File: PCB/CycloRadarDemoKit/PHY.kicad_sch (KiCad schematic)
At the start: 34 parts, among them J201 ARJM11B1-009-AB-EW2, U201 IP101GRI, Y201 25MHz

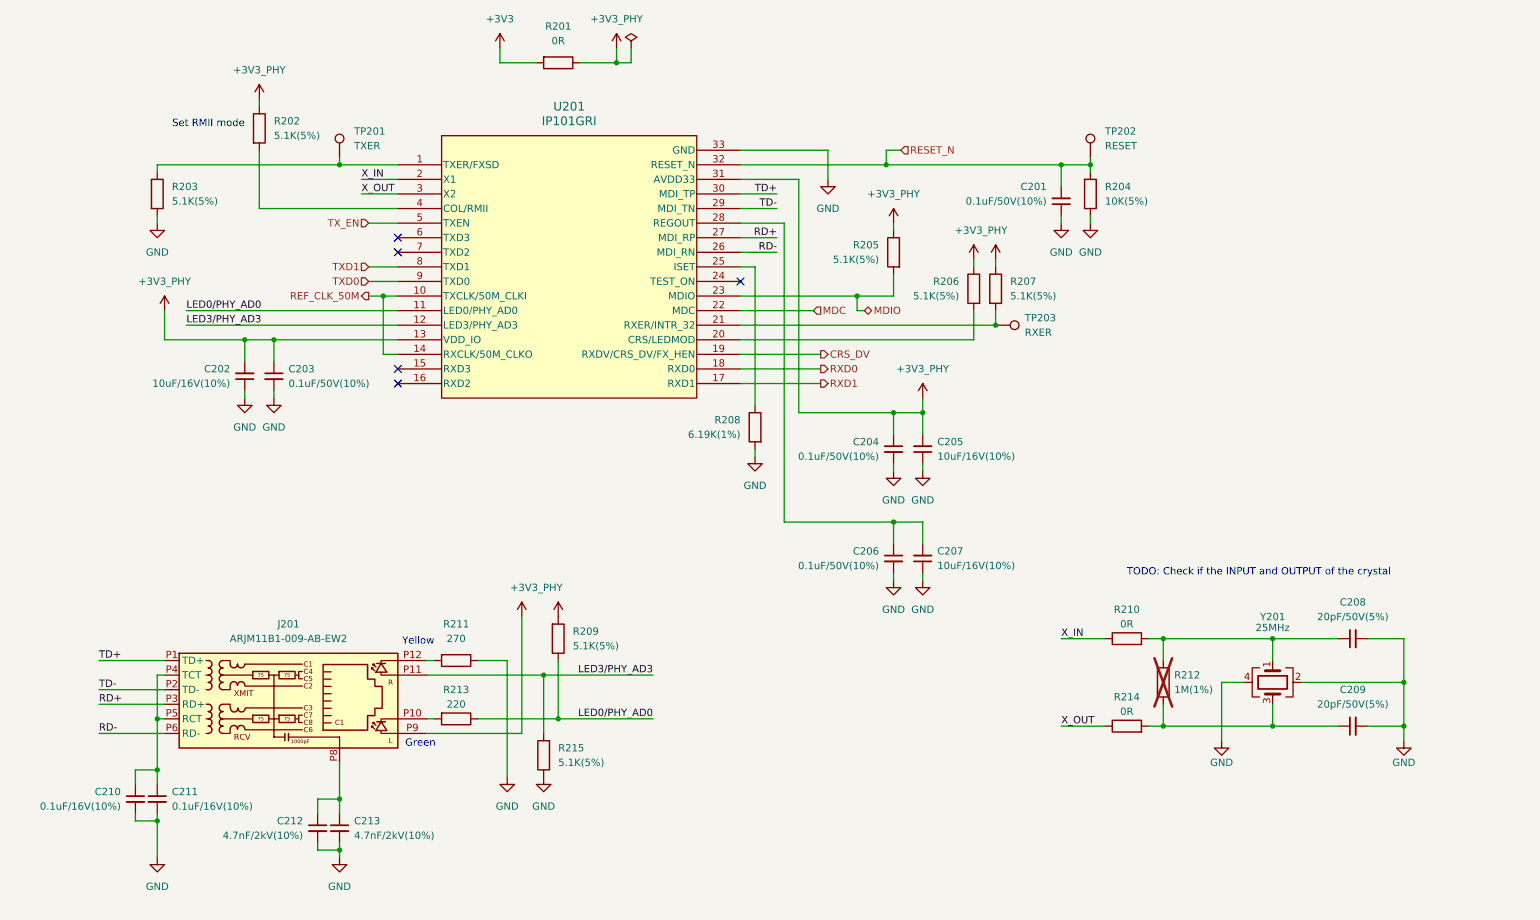
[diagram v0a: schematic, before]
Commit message: added buzzer and pins for Radar
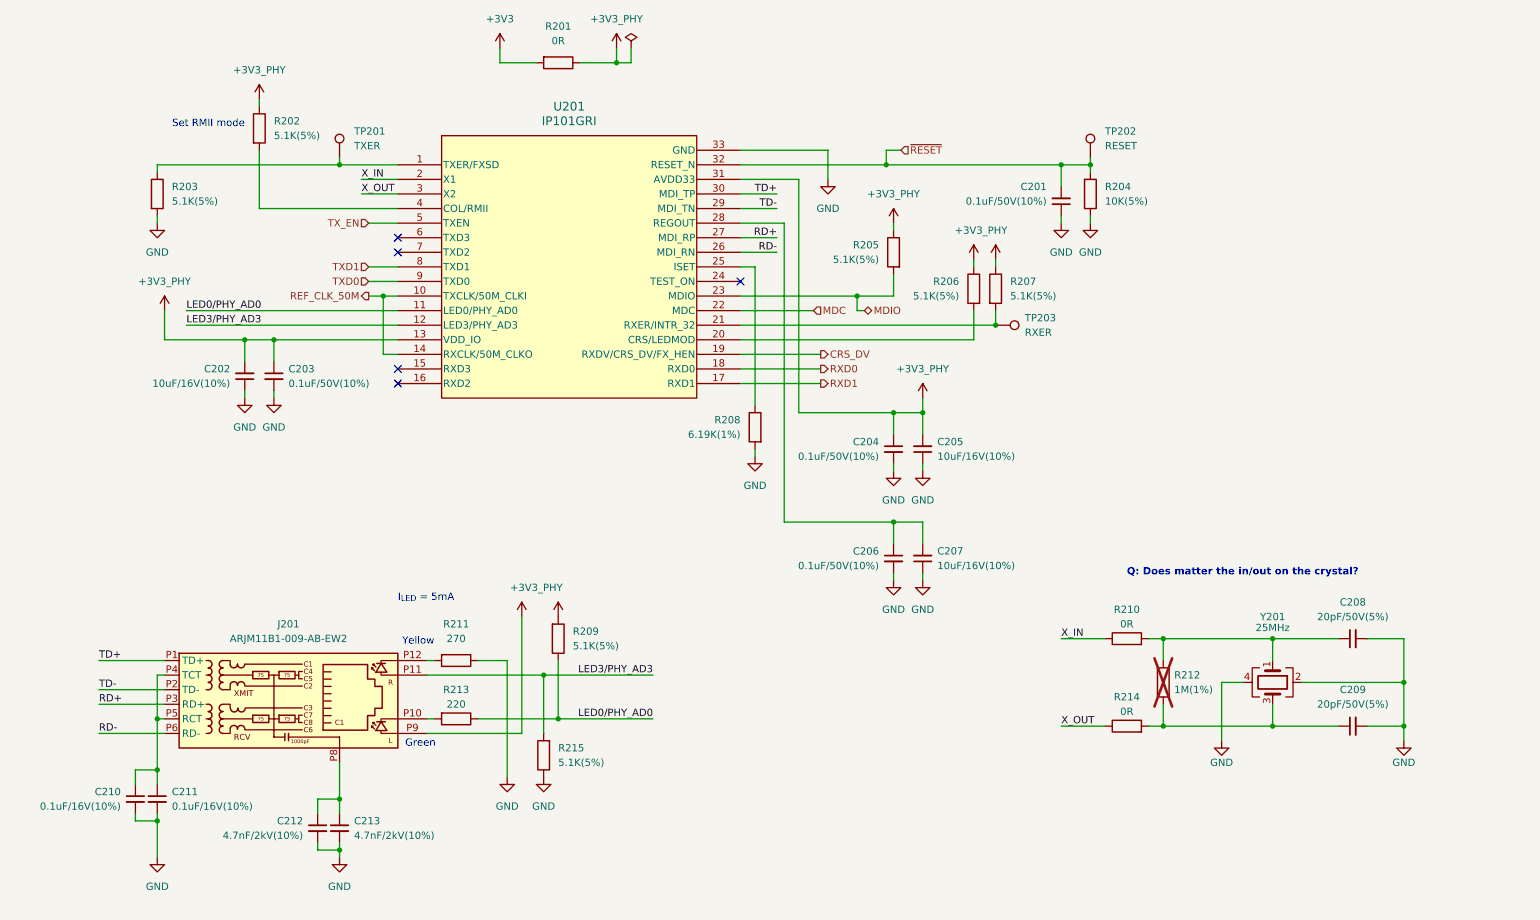
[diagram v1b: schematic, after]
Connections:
- net RESET_N renamed ~{RESET}
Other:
- note added: "I_{LED} = 5mA"
- note added: "Q: Does matter the in/out on the crystal?"
- note removed: "TODO: Check if the INPUT and OUTPUT of the crystal"
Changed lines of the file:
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@@
+    (effects (font (size 1.27 1.27)) (justify left bottom))
+  )
+  (text "I_{LED} = 5mA" (at 91.44 125.73 0)
     (effects (font (size 1.27 1.27)) (justify left bottom))
   )
@@
     (effects (font (size 1.27 1.27)) (justify right bottom))
   )
-  (text "TODO: Check if the INPUT and OUTPUT of the crystal"
-    (at 218.44 121.285 0)
-    (effects (font (size 1.27 1.27)) (justify left bottom))
+  (text "Q: Does matter the in/out on the crystal?" (at 218.44 121.285 0)
+    (effects (font (size 1.27 1.27) (thickness 0.254) bold) (justify left bottom))
   )
   (label "X_IN" (at 85.09 52.07 0) (fields_autoplaced)
@@
     (effects (font (size 1.27 1.27)) (justify right))
   )
-  (hierarchical_label "RESET_N" (shape input) (at 179.07 46.99 0) (fields_autoplaced)
+  (hierarchical_label "~{RESET}" (shape input) (at 179.07 46.99 0) (fields_autoplaced)
     (effects (font (size 1.27 1.27)) (justify left))
   )

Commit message: more components fthprnt added
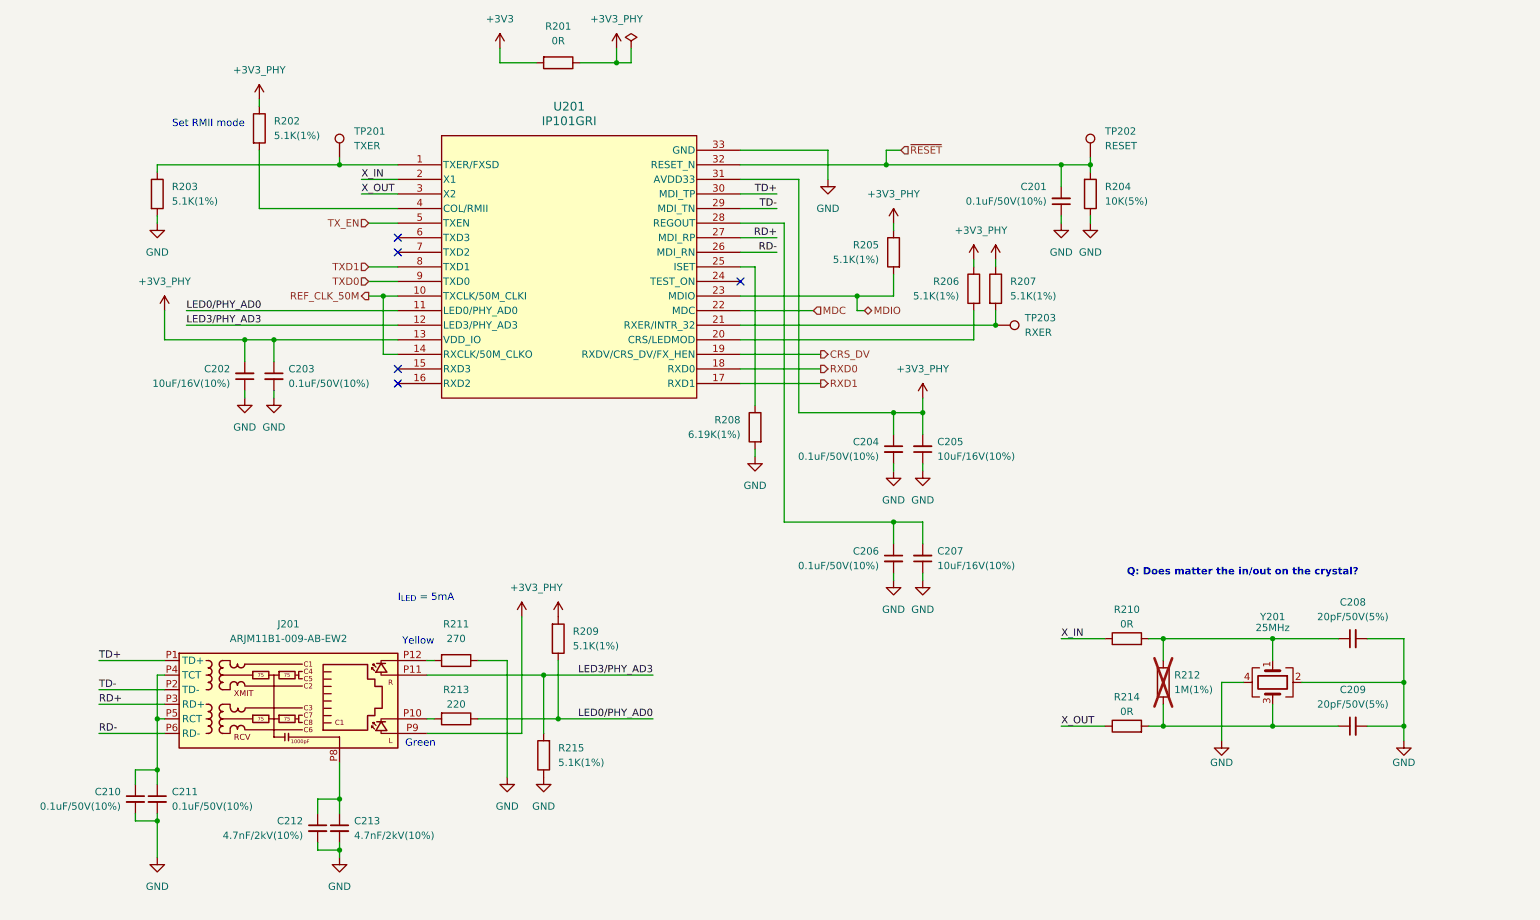
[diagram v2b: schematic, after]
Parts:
- C210, C211: value 0.1uF/16V(10%) -> 0.1uF/50V(10%); footprint (none) -> Capacitor_SMD:C_0603_1608Metric; LCSC (none) -> C14663
- R202, R203, R205, R206, R207, R209, R215: value 5.1K(5%) -> 5.1K(1%); footprint (none) -> Resistor_SMD:R_0603_1608Metric; LCSC (none) -> C23186
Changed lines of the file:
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@@
       (effects (font (size 1.27 1.27)) (justify right))
     )
-    (property "Value" "5.1K(5%)" (at 119.38 153.67 0)
+    (property "Value" "5.1K(1%)" (at 119.38 153.67 0)
       (effects (font (size 1.27 1.27)) (justify right))
     )
-    (property "Footprint" "" (at 118.618 152.4 90)
+    (property "Footprint" "Resistor_SMD:R_0603_1608Metric" (at 118.618 152.4 90)
       (effects (font (size 1.27 1.27)) hide)
     )
@@
       (effects (font (size 1.27 1.27)) hide)
     )
+    (property "LCSC" "C23186" (at 116.84 152.4 0)
+      (effects (font (size 1.27 1.27)) hide)
+    )
     (pin "1")
     (pin "2")
@@
       (effects (font (size 1.27 1.27)) (justify left))
     )
-    (property "Value" "5.1K(5%)" (at 121.92 133.35 0)
-      (effects (font (size 1.27 1.27)) (justify left))
-    )
-    (property "Footprint" "" (at 117.602 132.08 90)
+    (property "Value" "5.1K(1%)" (at 121.92 133.35 0)
+      (effects (font (size 1.27 1.27)) (justify left))
+    )
+    (property "Footprint" "Resistor_SMD:R_0603_1608Metric" (at 117.602 132.08 90)
       (effects (font (size 1.27 1.27)) hide)
     )
     (property "Datasheet" "~" (at 119.38 132.08 0)
+      (effects (font (size 1.27 1.27)) hide)
+    )
+    (property "LCSC" "C23186" (at 119.38 132.08 0)
       (effects (font (size 1.27 1.27)) hide)
     )
@@
       (effects (font (size 1.27 1.27)) (justify left))
     )
-    (property "Value" "5.1K(5%)" (at 175.26 66.04 0)
-      (effects (font (size 1.27 1.27)) (justify left))
-    )
-    (property "Footprint" "" (at 179.578 64.77 90)
+    (property "Value" "5.1K(1%)" (at 175.26 66.04 0)
+      (effects (font (size 1.27 1.27)) (justify left))
+    )
+    (property "Footprint" "Resistor_SMD:R_0603_1608Metric" (at 179.578 64.77 90)
       (effects (font (size 1.27 1.27)) hide)
     )
@@
       (effects (font (size 1.27 1.27)) hide)
     )
+    (property "LCSC" "C23186" (at 177.8 64.77 0)
+      (effects (font (size 1.27 1.27)) hide)
+    )
     (pin "1")
     (pin "2")
@@
       (effects (font (size 1.27 1.27)) (justify left))
     )
-    (property "Value" "5.1K(5%)" (at 52.07 55.88 0)
-      (effects (font (size 1.27 1.27)) (justify left))
-    )
-    (property "Footprint" "" (at 47.752 54.61 90)
+    (property "Value" "5.1K(1%)" (at 52.07 55.88 0)
+      (effects (font (size 1.27 1.27)) (justify left))
+    )
+    (property "Footprint" "Resistor_SMD:R_0603_1608Metric" (at 47.752 54.61 90)
       (effects (font (size 1.27 1.27)) hide)
     )
     (property "Datasheet" "~" (at 49.53 54.61 0)
+      (effects (font (size 1.27 1.27)) hide)
+    )
+    (property "LCSC" "C23186" (at 49.53 54.61 0)
       (effects (font (size 1.27 1.27)) hide)
     )
@@
       (effects (font (size 1.27 1.27)) (justify left))
     )
-    (property "Value" "5.1K(5%)" (at 198.12 72.39 0)
-      (effects (font (size 1.27 1.27)) (justify left))
-    )
-    (property "Footprint" "" (at 193.802 71.12 90)
+    (property "Value" "5.1K(1%)" (at 198.12 72.39 0)
+      (effects (font (size 1.27 1.27)) (justify left))
+    )
+    (property "Footprint" "Resistor_SMD:R_0603_1608Metric" (at 193.802 71.12 90)
       (effects (font (size 1.27 1.27)) hide)
     )
     (property "Datasheet" "~" (at 195.58 71.12 0)
+      (effects (font (size 1.27 1.27)) hide)
+    )
+    (property "LCSC" "C23186" (at 195.58 71.12 0)
       (effects (font (size 1.27 1.27)) hide)
     )
@@
       (effects (font (size 1.27 1.27)) (justify left))
     )
-    (property "Value" "0.1uF/16V(10%)" (at 52.07 161.2963 0)
-      (effects (font (size 1.27 1.27)) (justify left))
-    )
-    (property "Footprint" "" (at 49.53 160.02 0)
+    (property "Value" "0.1uF/50V(10%)" (at 52.07 161.2963 0)
+      (effects (font (size 1.27 1.27)) (justify left))
+    )
+    (property "Footprint" "Capacitor_SMD:C_0603_1608Metric" (at 49.53 160.02 0)
       (effects (font (size 1.27 1.27)) hide)
     )
     (property "Datasheet" "~" (at 49.53 160.02 0)
+      (effects (font (size 1.27 1.27)) hide)
+    )
+    (property "LCSC" "C14663" (at 49.53 160.02 0)
       (effects (font (size 1.27 1.27)) hide)
     )
@@
       (effects (font (size 1.27 1.27)) (justify left))
     )
-    (property "Value" "5.1K(5%)" (at 69.85 44.45 0)
-      (effects (font (size 1.27 1.27)) (justify left))
-    )
-    (property "Footprint" "" (at 65.532 43.18 90)
+    (property "Value" "5.1K(1%)" (at 69.85 44.45 0)
+      (effects (font (size 1.27 1.27)) (justify left))
+    )
+    (property "Footprint" "Resistor_SMD:R_0603_1608Metric" (at 65.532 43.18 90)
       (effects (font (size 1.27 1.27)) hide)
     )
     (property "Datasheet" "~" (at 67.31 43.18 0)
+      (effects (font (size 1.27 1.27)) hide)
+    )
+    (property "LCSC" "C23186" (at 67.31 43.18 0)
       (effects (font (size 1.27 1.27)) hide)
     )
@@
       (effects (font (size 1.27 1.27)) (justify left))
     )
-    (property "Value" "5.1K(5%)" (at 189.23 72.39 0)
-      (effects (font (size 1.27 1.27)) (justify left))
-    )
-    (property "Footprint" "" (at 193.548 71.12 90)
+    (property "Value" "5.1K(1%)" (at 189.23 72.39 0)
+      (effects (font (size 1.27 1.27)) (justify left))
+    )
+    (property "Footprint" "Resistor_SMD:R_0603_1608Metric" (at 193.548 71.12 90)
       (effects (font (size 1.27 1.27)) hide)
     )
     (property "Datasheet" "~" (at 191.77 71.12 0)
+      (effects (font (size 1.27 1.27)) hide)
+    )
+    (property "LCSC" "C23186" (at 191.77 71.12 0)
       (effects (font (size 1.27 1.27)) hide)
     )
@@
       (effects (font (size 1.27 1.27)) (justify left))
     )
-    (property "Value" "0.1uF/16V(10%)" (at 43.18 161.2963 0)
-      (effects (font (size 1.27 1.27)) (justify left))
-    )
-    (property "Footprint" "" (at 45.72 160.02 0)
+    (property "Value" "0.1uF/50V(10%)" (at 43.18 161.2963 0)
+      (effects (font (size 1.27 1.27)) (justify left))
+    )
+    (property "Footprint" "Capacitor_SMD:C_0603_1608Metric" (at 45.72 160.02 0)
       (effects (font (size 1.27 1.27)) hide)
     )
@@
       (effects (font (size 1.27 1.27)) hide)
     )
+    (property "LCSC" "C14663" (at 45.72 160.02 0)
+      (effects (font (size 1.27 1.27)) hide)
+    )

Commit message: added more LCSC parts
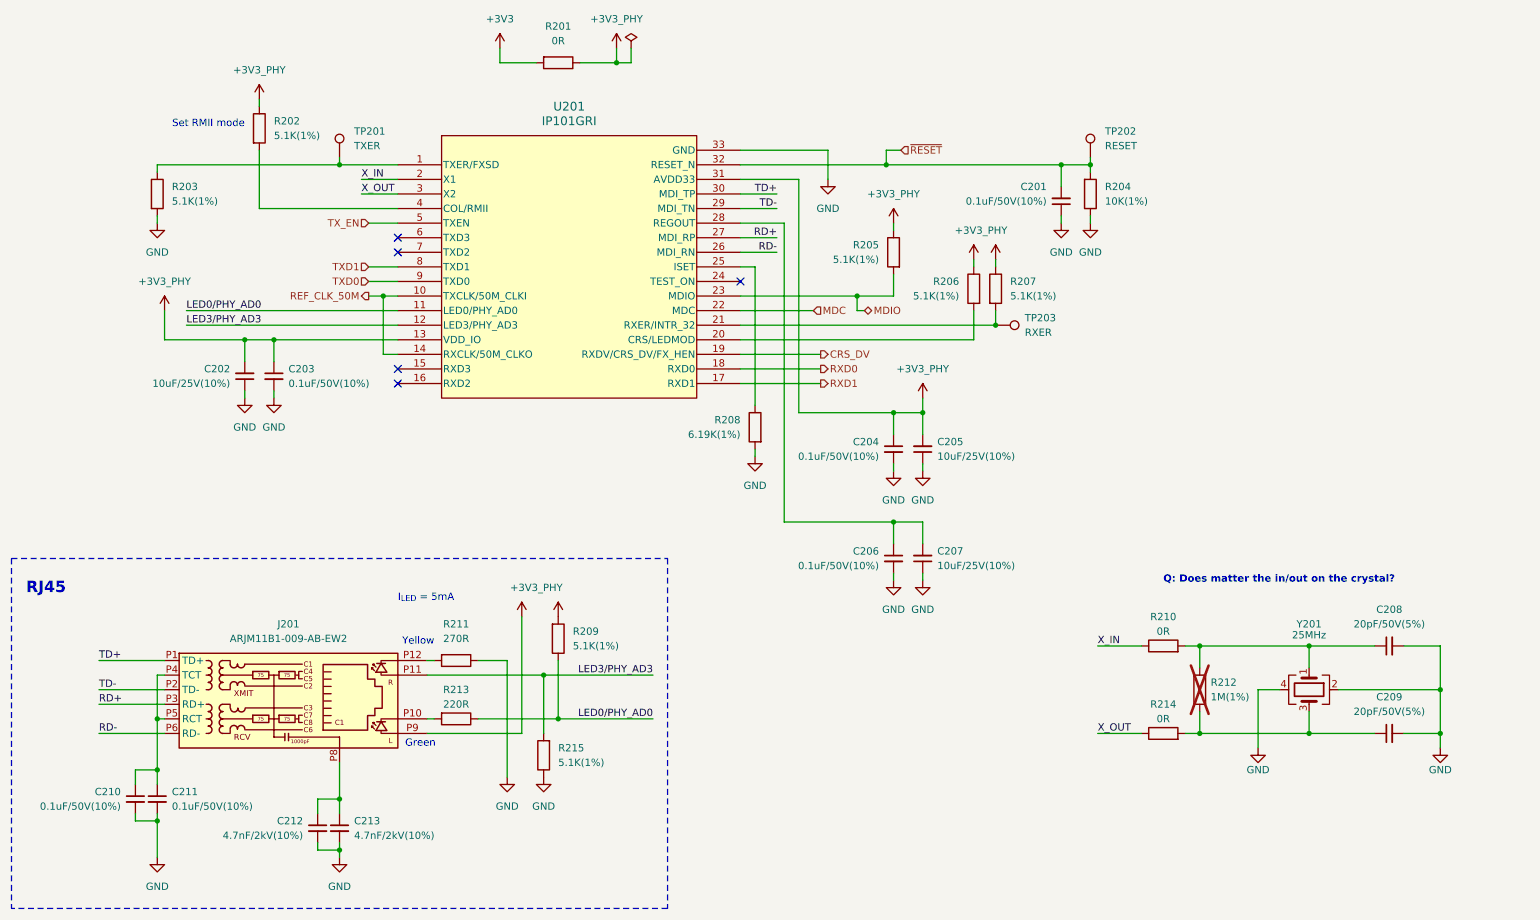
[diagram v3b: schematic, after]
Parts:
- C202, C205, C207: value 10uF/16V(10%) -> 10uF/25V(10%); footprint (none) -> Capacitor_SMD:C_1206_3216Metric; LCSC (none) -> C77090
- C212, C213: footprint (none) -> Capacitor_SMD:C_1206_3216Metric; LCSC (none) -> C41017
- R204: value 10K(5%) -> 10K(1%); footprint (none) -> Resistor_SMD:R_0603_1608Metric; LCSC (none) -> C25804
- R208: footprint (none) -> Resistor_SMD:R_0603_1608Metric; LCSC (none) -> C403300
- R211: value 270 -> 270R
- R212: footprint (none) -> Resistor_SMD:R_0603_1608Metric; LCSC (none) -> C22935
- R213: value 220 -> 220R
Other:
- note added: "RJ45"
- moved on the sheet: C208, C209, R210, R212, R214, Y201

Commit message: PCB ready for review
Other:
- note added: "100Base-TX RJ45"
- note added: "25MHz crystal"
- note removed: "RJ45"
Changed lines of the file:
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@@
     (stroke (width 0) (type default))
+  )
+  (polyline (pts (xy 208.28 160.02) (xy 278.13 160.02))
+    (stroke (width 0) (type dash))
   )
   (polyline (pts (xy 138.43 118.11) (xy 138.43 179.07))
@@
     (stroke (width 0) (type default))
   )
+  (polyline (pts (xy 278.13 160.02) (xy 278.13 118.11))
+    (stroke (width 0) (type dash))
+  )
   (wire (pts (xy 250.19 133.35) (xy 261.62 133.35))
     (stroke (width 0) (type default))
@@
     (stroke (width 0) (type dash))
   )
+  (polyline (pts (xy 208.28 118.11) (xy 208.28 160.02))
+    (stroke (width 0) (type dash))
+  )
   (wire (pts (xy 241.3 140.97) (xy 241.3 151.13))
     (stroke (width 0) (type default))
@@
   (wire (pts (xy 77.47 160.02) (xy 81.28 160.02))
     (stroke (width 0) (type default))
+  )
+  (polyline (pts (xy 208.28 118.11) (xy 278.13 118.11))
+    (stroke (width 0) (type dash))
   )
   (wire (pts (xy 212.09 49.53) (xy 207.01 49.53))
@@
     (effects (font (size 1.27 1.27)) (justify left bottom))
   )
-  (text "RJ45" (at 26.67 124.46 0)
+  (text "100Base-TX RJ45" (at 26.67 124.46 0)
     (effects (font (size 2 2) (thickness 0.4) bold) (justify left bottom))
   )
@@
     (effects (font (size 1.27 1.27)) (justify left bottom))
   )
+  (text "25MHz crystal" (at 210.82 123.19 0)
+    (effects (font (size 2 2) (thickness 0.4) bold) (justify left bottom))
+  )
   (text "Set RMII mode" (at 64.77 43.18 0)
     (effects (font (size 1.27 1.27)) (justify right bottom))
@@
     (effects (font (size 1.27 1.27)) (justify right bottom))
   )
-  (text "Q: Does matter the in/out on the crystal?" (at 224.79 122.555 0)
+  (text "Q: Does matter the in/out on the crystal?" (at 237.49 115.57 0)
     (effects (font (size 1.27 1.27) (thickness 0.254) bold) (justify left bottom))
   )

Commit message: PCB after review
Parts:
- C201, C210, C211: value 0.1uF/50V(10%) -> 100nF/50V(10%)
- C203, C204, C206: value 0.1uF/50V(10%) -> 1uF/50V(10%); LCSC C14663 -> C15849
- TP201, TP202, TP203: footprint (none) -> TestPoint:TestPoint_Pad_D2.0mm
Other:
- note added: "Receive error"
- note added: "To define standard current of intrenal circuit"
- note added: "Transmit enable"
- note removed: "Q: Does matter the in/out on the crystal?"
- company: Alps Electric Czech, s.r.o. -> ALPS Electric Czech, s.r.o.
- title: Development module for Radar Safety Sensor -> Safety Ride Radar Sensor
- moved on the sheet: C201, R204, R205, R206, R207, TP202, TP203
